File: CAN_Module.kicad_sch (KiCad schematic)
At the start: 14 parts, among them U3 SN65HVD231

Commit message: pre remobing sd card
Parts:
- removed TP4, TP5: TestPoint, TestPoint:TestPoint_Pad_D2.0mm, symbol Connector:TestPoint
- TP1, TP10: footprint TestPoint:TestPoint_Pad_D2.0mm -> TestPoint:TestPoint_Pad_D1.5mm

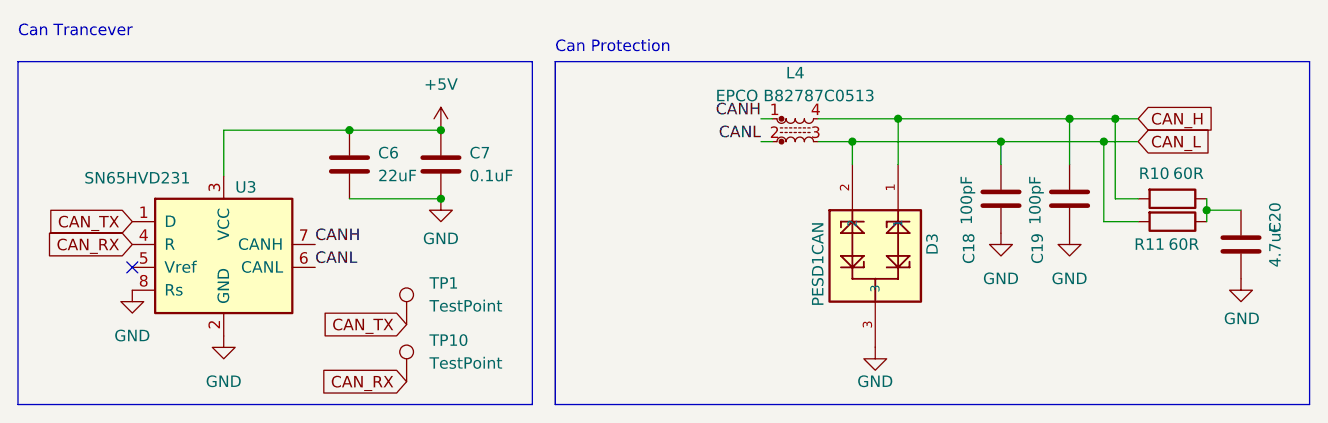
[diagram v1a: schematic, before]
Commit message: switchen can supply to 3v3
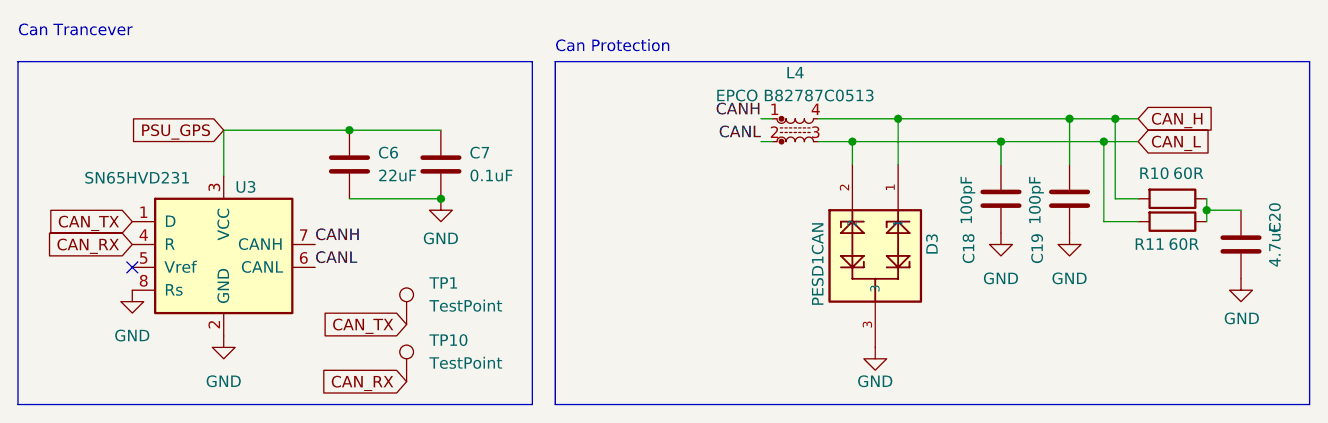
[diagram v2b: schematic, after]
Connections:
- net +5V renamed PSU_GPS
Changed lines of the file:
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@@
 	(paper "A4")
-	(junction
-		(at 64.77 25.4)
-		(diameter 0)
-		(color 0 0 0 0)
-	)
 	(junction
 		(at 134.62 24.13)
@@
 		)
 	)
+	(global_label "PSU_GPS"
+		(shape input)
+		(at 40.64 25.4 180)
+		(fields_autoplaced yes)
+		(effects
+			(font
+				(size 1.27 1.27)
+			)
+			(justify right)
+		)
+		(property "Intersheetrefs" "${INTERSHEET_REFS}"
+			(at 29.1277 25.4 0)
+			(effects
+				(font
+					(size 1.27 1.27)
+				)
+				(justify right)
+				(hide yes)
+			)
+		)
+	)
 	(global_label "CAN_H"
 		(shape input)
@@
 			)
 		)
-	)
-	(symbol
-		(lib_id "power:+5V")
-		(at 64.77 25.4 0)
-		(mirror y)
-		(unit 1)
-		(exclude_from_sim no)
-		(in_bom yes)
-		(on_board yes)
-		(dnp no)
-		(fields_autoplaced yes)
-		(property "Reference" "#PWR014"
-			(at 64.77 29.21 0)
-			(effects
-				(font
-					(size 1.27 1.27)
-				)
-				(hide yes)
-			)
-		)
-		(property "Value" "+5V"
-			(at 64.77 20.32 0)
-			(effects
-				(font
-					(size 1.27 1.27)
-				)
-			)
-		)
-		(property "Footprint" ""
-			(at 64.77 25.4 0)
-			(effects
-				(font
-					(size 1.27 1.27)
-				)
-				(hide yes)
-			)
-		)
-		(property "Datasheet" ""
-			(at 64.77 25.4 0)
-			(effects
-				(font
-					(size 1.27 1.27)
-				)
-				(hide yes)
-			)
-		)
-		(property "Description" ""
-			(at 64.77 25.4 0)
-			(effects
-				(font
-					(size 1.27 1.27)
-				)
-				(hide yes)
-			)
-		)
-		(pin "1"
-		)
-		(instances
-			(project "Hardware"
-				(path "/f04ee758-a926-48b7-b458-286a696c3ef4/3ee8d0fa-24f8-4e27-8de4-cc9f5f0f11cc"
-					(reference "#PWR014")
-					(unit 1)
-				)
-			)
-		)

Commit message: first new layout
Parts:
- removed TP1, TP10: TestPoint, TestPoint:TestPoint_Pad_D1.5mm, symbol Connector:TestPoint
- C7: value 0.1uF -> 100nF
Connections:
- net PSU_GPS renamed +3V3
